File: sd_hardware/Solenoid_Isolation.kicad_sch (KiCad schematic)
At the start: 44 parts, among them Q1 RD3L08BGNTL, Q2 RD3L08BGNTL, Q3 RD3L08BGNTL, Q4 RD3L08BGNTL, Q5 RD3L08BGNTL, Q6 RD3L08BGNTL, Q7 RD3L08BGNTL, Q8 RD3L08BGNTL, U1 TLP291, U2 TLP291, U3 TLP291, U4 TLP291, U5 TLP291, U6 TLP291, U7 TLP291, U8 TLP291

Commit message: fix
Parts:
- D1: renamed from D3; footprint (none) -> LED_SMD:LED_0603_1608Metric_Pad1.05x0.95mm_HandSolder
- D10: renamed from D15; footprint (none) -> Diode_SMD:D_SOD-128
- D11: renamed from D8; footprint (none) -> Diode_SMD:D_SOD-128
- D12: renamed from D16; footprint (none) -> Diode_SMD:D_SOD-128
- D13: renamed from D9; footprint (none) -> Diode_SMD:D_SOD-128
- D14: renamed from D17; footprint (none) -> Diode_SMD:D_SOD-128
- D15: renamed from D10; footprint (none) -> Diode_SMD:D_SOD-128
- D16: renamed from D18; footprint (none) -> Diode_SMD:D_SOD-128
- D2: renamed from D11; footprint (none) -> LED_SMD:LED_0603_1608Metric_Pad1.05x0.95mm_HandSolder
- D3: renamed from D4; footprint (none) -> LED_SMD:LED_0603_1608Metric_Pad1.05x0.95mm_HandSolder
- D4: renamed from D12; footprint (none) -> LED_SMD:LED_0603_1608Metric_Pad1.05x0.95mm_HandSolder
- D5: footprint (none) -> LED_SMD:LED_0603_1608Metric_Pad1.05x0.95mm_HandSolder
- D6: renamed from D13; footprint (none) -> LED_SMD:LED_0603_1608Metric_Pad1.05x0.95mm_HandSolder
- D7: renamed from D6; footprint (none) -> LED_SMD:LED_0603_1608Metric_Pad1.05x0.95mm_HandSolder
- D8: renamed from D14; footprint (none) -> LED_SMD:LED_0603_1608Metric_Pad1.05x0.95mm_HandSolder
- D9: renamed from D7; footprint (none) -> Diode_SMD:D_SOD-128
- Q1, Q8: footprint (none) -> y-robo_footprint:TO252-3_ROM
- Q2: renamed from Q5; footprint (none) -> y-robo_footprint:TO252-3_ROM
- Q3: renamed from Q2; footprint (none) -> y-robo_footprint:TO252-3_ROM
- Q4: renamed from Q6; footprint (none) -> y-robo_footprint:TO252-3_ROM
- Q5: renamed from Q3; footprint (none) -> y-robo_footprint:TO252-3_ROM
- Q6: renamed from Q7; footprint (none) -> y-robo_footprint:TO252-3_ROM
- Q7: renamed from Q4; footprint (none) -> y-robo_footprint:TO252-3_ROM
- R1: renamed from R4; footprint (none) -> Resistor_SMD:R_0603_1608Metric_Pad0.98x0.95mm_HandSolder
- R2: renamed from R8; footprint (none) -> Resistor_SMD:R_0603_1608Metric_Pad0.98x0.95mm_HandSolder
- R3: renamed from R5; footprint (none) -> Resistor_SMD:R_0603_1608Metric_Pad0.98x0.95mm_HandSolder
- R4: renamed from R9; footprint (none) -> Resistor_SMD:R_0603_1608Metric_Pad0.98x0.95mm_HandSolder
- R5: renamed from R6; footprint (none) -> Resistor_SMD:R_0603_1608Metric_Pad0.98x0.95mm_HandSolder
- R6: renamed from R10; footprint (none) -> Resistor_SMD:R_0603_1608Metric_Pad0.98x0.95mm_HandSolder
- R7: footprint (none) -> Resistor_SMD:R_0603_1608Metric_Pad0.98x0.95mm_HandSolder
- R8: renamed from R11; footprint (none) -> Resistor_SMD:R_0603_1608Metric_Pad0.98x0.95mm_HandSolder
- RN1: renamed from RN2; footprint (none) -> Resistor_SMD:R_Array_Convex_8x0602
- RN2: renamed from RN1; footprint (none) -> Resistor_SMD:R_Array_Convex_8x0602
- RN3, RN4: footprint (none) -> Resistor_SMD:R_Array_Convex_8x0602
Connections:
- net FET1_Gate: now also RN3.9 (R8.2), RN4.1 (R1.1); no longer RN3.8 (R8.1), RN4.8 (R8.1)
- net FET2_Gate: now also Q2.1 (G), RN3.10 (R7.2), RN4.2 (R2.1); no longer Q3.1 (G), RN3.7 (R7.1), RN4.7 (R7.1)
- net FET3_Gate: now also Q3.1 (G), RN3.11 (R6.2), RN4.3 (R3.1); no longer Q5.1 (G), RN3.6 (R6.1), RN4.6 (R6.1)
- net FET4_Gate: now also Q4.1 (G), RN3.12 (R5.2), RN4.4 (R4.1); no longer Q7.1 (G), RN3.5 (R5.1), RN4.5 (R5.1)
- net FET5_Gate: now also Q5.1 (G), RN3.13 (R4.2), RN4.5 (R5.1); no longer Q2.1 (G), RN3.4 (R4.1), RN4.4 (R4.1)
- net FET6_Gate: now also Q6.1 (G), RN3.14 (R3.2), RN4.6 (R6.1); no longer Q4.1 (G), RN3.3 (R3.1), RN4.3 (R3.1)
- net FET7_Gate: now also Q7.1 (G), RN3.15 (R2.2), RN4.7 (R7.1); no longer Q6.1 (G), RN3.2 (R2.1), RN4.2 (R2.1)
- net FET8_Gate: now also RN3.16 (R1.2), RN4.8 (R8.1); no longer RN3.1 (R1.1), RN4.1 (R1.1)
- net GPIO1_IN: now also RN2.8 (R8.1); no longer RN2.9 (R8.2)
- net GPIO2_IN: now also RN2.7 (R7.1); no longer RN2.10 (R7.2)
- net GPIO3_IN: now also RN2.6 (R6.1); no longer RN2.11 (R6.2)
- net GPIO4_IN: now also RN2.5 (R5.1); no longer RN2.12 (R5.2)
- net GPIO5_IN: now also RN2.4 (R4.1); no longer RN2.13 (R4.2)
- net GPIO6_IN: now also RN2.3 (R3.1); no longer RN2.14 (R3.2)
- net GPIO7_IN: now also RN2.2 (R2.1); no longer RN2.15 (R2.2)
- net GPIO8_IN: now also RN2.1 (R1.1); no longer RN2.16 (R1.2)
- net Solenoid2_-: now also D10.2 (A), D2.1 (K), Q2.2 (D); no longer D11.2 (A), D3.1 (K), Q3.2 (D)
- net Solenoid3_-: now also D11.2 (A), D3.1 (K), Q3.2 (D); no longer D13.2 (A), D5.1 (K), Q5.2 (D)
- net Solenoid4_-: now also D12.2 (A), D4.1 (K), Q4.2 (D); no longer D15.2 (A), D7.1 (K), Q7.2 (D)
- net Solenoid5_-: now also D13.2 (A), D5.1 (K), Q5.2 (D); no longer D10.2 (A), D2.1 (K), Q2.2 (D)
- net Solenoid6_-: now also D14.2 (A), D6.1 (K), Q6.2 (D); no longer D12.2 (A), D4.1 (K), Q4.2 (D)
- net Solenoid7_-: now also D15.2 (A), D7.1 (K), Q7.2 (D); no longer D14.2 (A), D6.1 (K), Q6.2 (D)
- net at U2.1: now also RN2.10 (R7.2); no longer RN2.7 (R7.1)
- net at U2.3: now also RN3.7 (R7.1); no longer RN3.10 (R7.2)
- net at U8.1: now also RN2.16 (R1.2); no longer RN2.1 (R1.1)
- net at U7.1: now also RN2.15 (R2.2); no longer RN2.2 (R2.1)
- net at U6.1: now also RN2.14 (R3.2); no longer RN2.3 (R3.1)
- net at U5.1: now also RN2.13 (R4.2); no longer RN2.4 (R4.1)
- net at U4.1: now also RN2.12 (R5.2); no longer RN2.5 (R5.1)
- net at U3.1: now also RN2.11 (R6.2); no longer RN2.6 (R6.1)
- net at U1.1: now also RN2.9 (R8.2); no longer RN2.8 (R8.1)
- net at U3.3: now also RN3.6 (R6.1); no longer RN3.11 (R6.2)
- net at U4.3: now also RN3.5 (R5.1); no longer RN3.12 (R5.2)
- net at U5.3: now also RN3.4 (R4.1); no longer RN3.13 (R4.2)
- net at U6.3: now also RN3.3 (R3.1); no longer RN3.14 (R3.2)
- net at U7.3: now also RN3.2 (R2.1); no longer RN3.15 (R2.2)
- net at U8.3: now also RN3.1 (R1.1); no longer RN3.16 (R1.2)
- net at U1.3: now also RN3.8 (R8.1); no longer RN3.9 (R8.2)
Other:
- moved on the sheet: RN2, RN3, RN4

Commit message: fix var3.0 sd_hardware
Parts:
- removed RN3: 120_x8, Resistor_SMD:R_Array_Convex_8x0602, symbol Device:R_Pack08
- added R13, R14, R15, R16, R17, R18, R19, R20: 120, Resistor_SMD:R_0603_1608Metric_Pad0.98x0.95mm_HandSolder, symbol Device:R
- R1, R2, R3, R4, R5, R6, R7, R8: value 1k -> 1.5k
- renumbered RN4 to RN3
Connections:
- net FET1_Gate: now also R13.1
- net FET2_Gate: now also R14.1
- net FET3_Gate: now also R15.1
- net FET4_Gate: now also R16.1
- net FET5_Gate: now also R17.1
- net FET6_Gate: now also R18.1
- net FET7_Gate: now also R19.1
- net FET8_Gate: now also R20.1
- net at U2.3: now also R14.2
- net at U8.3: now also R20.2
- net at U7.3: now also R19.2
- net at U6.3: now also R18.2
- net at U5.3: now also R17.2
- net at U4.3: now also R16.2
- net at U3.3: now also R15.2
- net at U1.3: now also R13.2

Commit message: delete RN
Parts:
- removed RN1: 1k_x8, Resistor_SMD:R_Array_Convex_8x0602, symbol Device:R_Pack08
- removed RN2: 330_x8, Resistor_SMD:R_Array_Convex_8x0602, symbol Device:R_Pack08
- removed RN3: 10k_x08, Resistor_SMD:R_Array_Convex_8x0602, symbol Device:R_Pack08
- added R22, R23, R24, R25, R26, R27, R28, R29: 330, Resistor_SMD:R_0603_1608Metric_Pad0.98x0.95mm_HandSolder, symbol Device:R
- added R30, R31, R32, R33, R34, R35, R36, R37: 1k, Resistor_SMD:R_0603_1608Metric_Pad0.98x0.95mm_HandSolder, symbol Device:R
- added R38, R39, R40, R41, R42, R43, R44, R45: 10k, Resistor_SMD:R_0603_1608Metric_Pad0.98x0.95mm_HandSolder, symbol Device:R
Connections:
- net +12V: now also R30.1, R31.1, R32.1, R33.1, R34.1, R35.1, R36.1, R37.1
- net FET1_Gate: now also R38.2
- net FET2_Gate: now also R39.2
- net FET3_Gate: now also R40.2
- net FET4_Gate: now also R41.2
- net FET5_Gate: now also R45.2
- net FET6_Gate: now also R44.2
- net FET7_Gate: now also R43.2
- net FET8_Gate: now also R42.2
- net GNDPWR: now also R38.1, R39.1, R40.1, R41.1, R42.1, R43.1, R44.1, R45.1
- net GPIO1_IN: now also R22.2
- net GPIO2_IN: now also R23.2
- net GPIO3_IN: now also R24.2
- net GPIO4_IN: now also R25.2
- net GPIO5_IN: now also R26.2
- net GPIO6_IN: now also R27.2
- net GPIO7_IN: now also R28.2
- net GPIO8_IN: now also R29.2
- net at U2.1: now also R23.1
- net at U2.4: now also R37.2
- net at U3.1: now also R24.1
- net at U4.1: now also R25.1
- net at U5.1: now also R26.1
- net at U6.1: now also R27.1
- net at U7.1: now also R28.1
- net at U8.1: now also R29.1
- net at U1.1: now also R22.1
- net at U3.4: now also R34.2
- net at U4.4: now also R35.2
- net at U8.4: now also R30.2
- net at U5.4: now also R32.2
- net at U6.4: now also R33.2
- net at U7.4: now also R31.2
- net at U1.4: now also R36.2

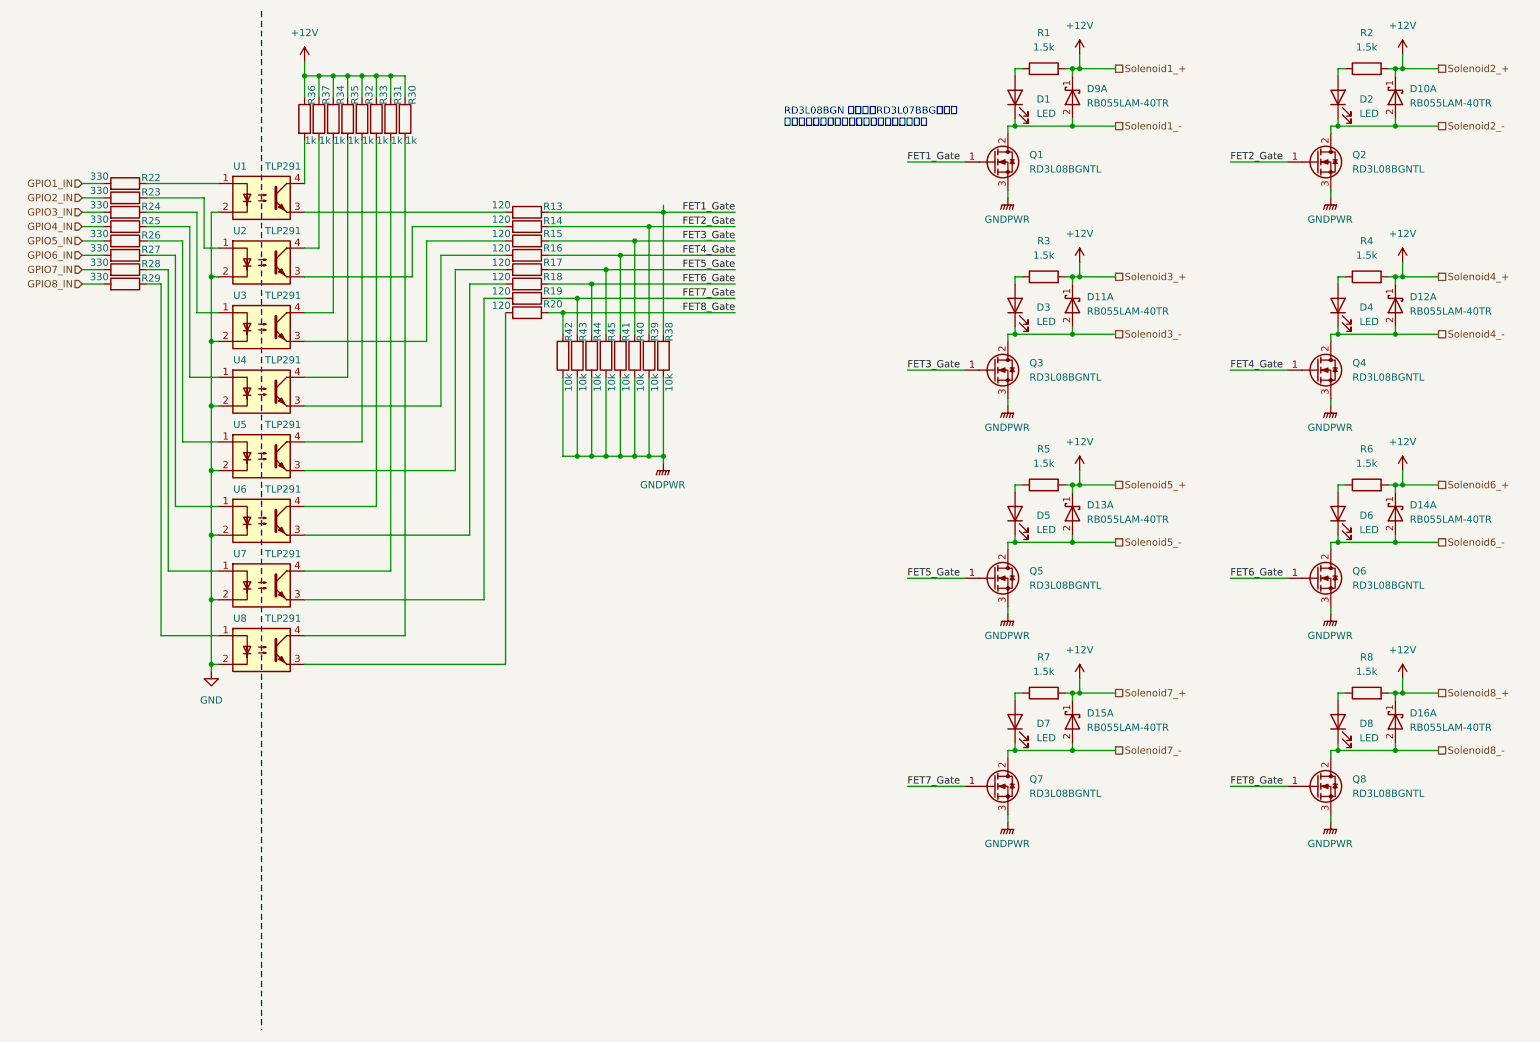
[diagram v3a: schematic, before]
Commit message: Change to Photo Relay
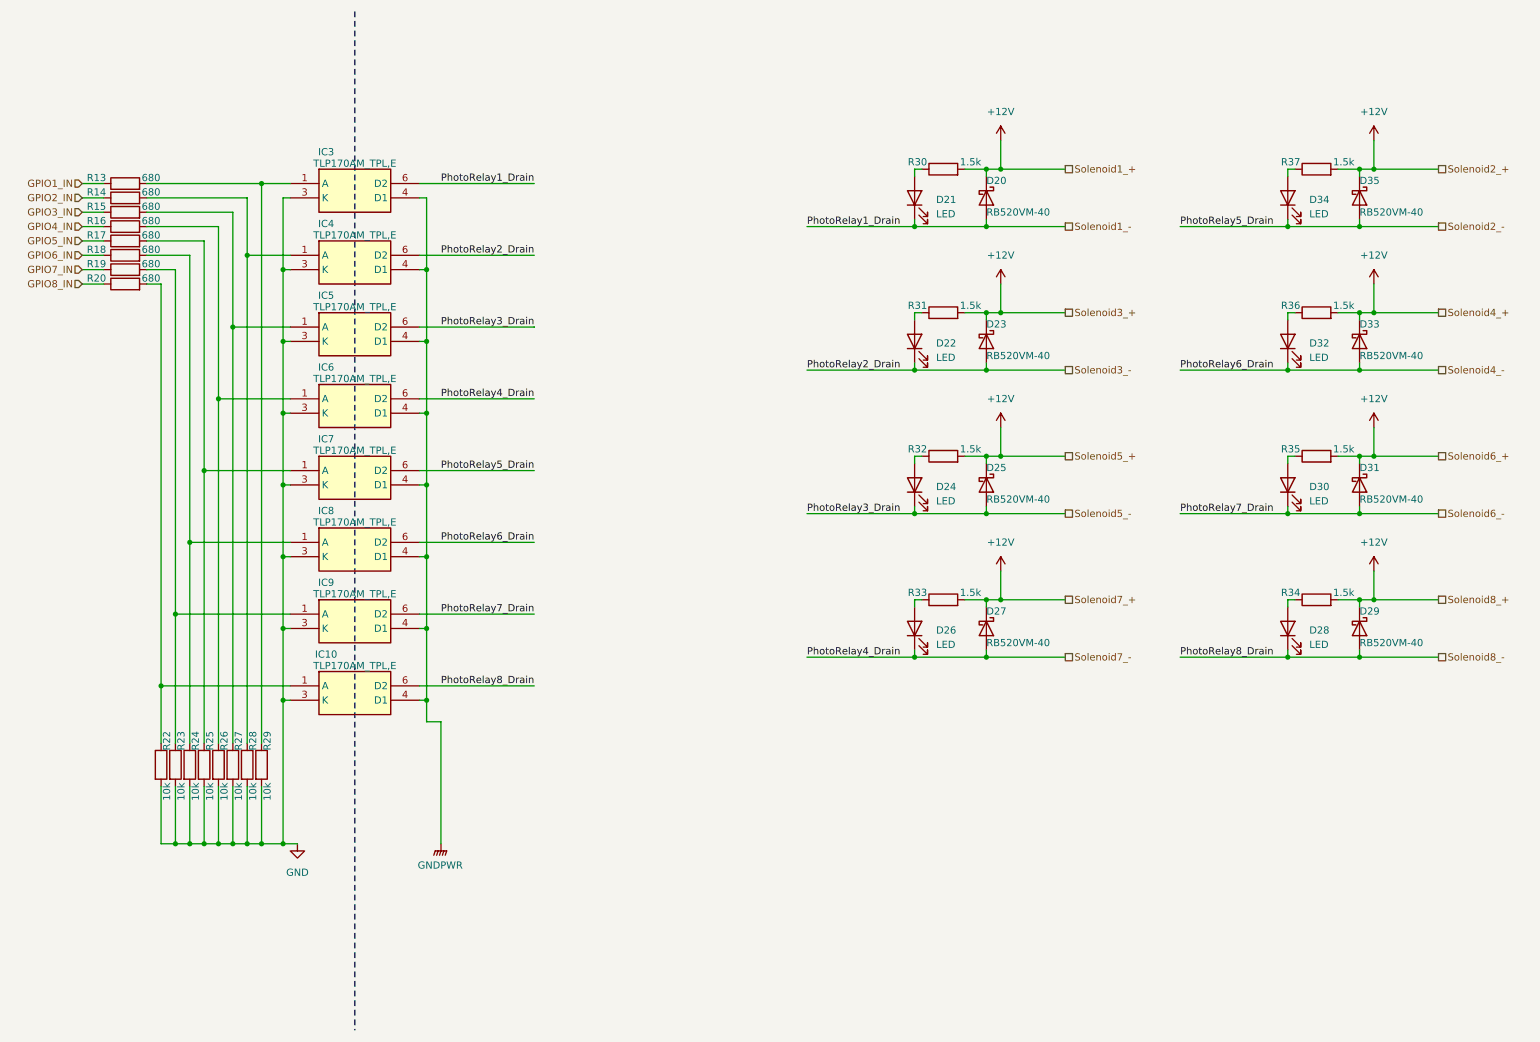
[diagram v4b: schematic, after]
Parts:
- removed D1, D2, D3, D4, D5, D6, D7, D8: LED, LED_SMD:LED_0603_1608Metric_Pad1.05x0.95mm_HandSolder, symbol Device:LED
- removed D10, D11, D12, D13, D14, D15, D16, D9: RB055LAM-40TR, Diode_SMD:D_SOD-128, symbol Device:D_Schottky_Dual_CommonAnode_KAK_Split
- removed Q1, Q2, Q3, Q4, Q5, Q6, Q7, Q8: RD3L08BGNTL, y-robo_footprint:TO252-3_ROM, symbol Transistor_FET:Q_NMOS_GDS
- removed R1, R2, R3, R4, R5, R6, R7, R8: 1.5k, Resistor_SMD:R_0603_1608Metric_Pad0.98x0.95mm_HandSolder, symbol Device:R
- removed R38, R39, R40, R41, R42, R43, R44, R45: 10k, Resistor_SMD:R_0603_1608Metric_Pad0.98x0.95mm_HandSolder, symbol Device:R
- removed U1, U2, U3, U4, U5, U6, U7, U8: TLP291, Package_SO:SOIC-4_4.55x2.6mm_P1.27mm, symbol Isolator:TLP291
- added D20, D23, D25, D27, D29, D31, D33, D35: RB520VM-40, Diode_THT:Diode_Bridge_Round_D9.0mm, symbol Device:D_Schottky
- added D21, D22, D24, D26, D28, D30, D32, D34: LED, LED_SMD:LED_0603_1608Metric_Pad1.05x0.95mm_HandSolder, symbol Device:LED
- added IC10, IC3, IC4, IC5, IC6, IC7, IC8, IC9: TLP170AM_TPL,E, TLP170AMTPLE, symbol TLP170AM_TPL_E:TLP170AM_TPL,E
- R13, R14, R15, R16, R17, R18, R19, R20: value 120 -> 680; footprint Resistor_SMD:R_0603_1608Metric_Pad0.98x0.95mm_HandSolder -> TLP170AMTPLE
- R22, R23, R24, R25, R26, R27, R28, R29: value 330 -> 10k; footprint Resistor_SMD:R_0603_1608Metric_Pad0.98x0.95mm_HandSolder -> TLP170AMTPLE
- R30, R31, R32, R33, R34, R35, R36, R37: value 1k -> 1.5k
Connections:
- net FET1_Gate is gone; now on net GPIO1_IN: R13.1
- net FET2_Gate is gone; now on net GPIO2_IN: R14.1
- net FET3_Gate is gone; now on net GPIO3_IN: R15.1
- net FET4_Gate is gone; now on net GPIO4_IN: R16.1
- net FET5_Gate is gone; now on net GPIO5_IN: R17.1
- net FET6_Gate is gone; now on net GPIO6_IN: R18.1
- net FET7_Gate is gone; now on net GPIO7_IN: R19.1
- net FET8_Gate is gone; now on net GPIO8_IN: R20.1
- net +12V: now also R30.2, R31.2, R32.2, R33.2, R34.2, R35.2, R36.2, R37.2, D20.1 (K), D23.1 (K), D25.1 (K), D27.1 (K), D29.1 (K), D31.1 (K), D33.1 (K), D35.1 (K); no longer R30.1, R31.1, R32.1, R33.1, R34.1, R35.1, R36.1, R37.1
- net GND: now also R22.2, R23.2, R24.2, R25.2, R26.2, R27.2, R28.2, R29.2, IC10.3 (K), IC3.3 (K), IC4.3 (K), IC5.3 (K), IC6.3 (K), IC7.3 (K), IC8.3 (K), IC9.3 (K)
- net GNDPWR: now also IC10.4 (D1), IC3.4 (D1), IC4.4 (D1), IC5.4 (D1), IC6.4 (D1), IC7.4 (D1), IC8.4 (D1), IC9.4 (D1)
- net GPIO1_IN: no longer R22.2
- net GPIO2_IN: no longer R23.2
- net GPIO3_IN: no longer R24.2
- net GPIO4_IN: no longer R25.2
- net GPIO5_IN: no longer R26.2
- net GPIO6_IN: no longer R27.2
- net GPIO7_IN: no longer R28.2
- net GPIO8_IN: no longer R29.2
- net Solenoid1_-: now also D20.2 (A), D21.1 (K), IC3.6 (D2)
- net Solenoid2_-: now also D34.1 (K), D35.2 (A), IC7.6 (D2)
- net Solenoid3_-: now also D22.1 (K), D23.2 (A), IC4.6 (D2)
- net Solenoid4_-: now also D32.1 (K), D33.2 (A), IC8.6 (D2)
- net Solenoid5_-: now also D24.1 (K), D25.2 (A), IC5.6 (D2)
- net Solenoid6_-: now also D30.1 (K), D31.2 (A), IC9.6 (D2)
- net Solenoid7_-: now also D26.1 (K), D27.2 (A), IC6.6 (D2)
- net Solenoid8_-: now also D28.1 (K), D29.2 (A), IC10.6 (D2)
- net at R15.2: now also R27.1, IC5.1 (A)
- net at R17.2: now also R25.1, IC7.1 (A)
- net at R13.2: now also R29.1, IC3.1 (A)
- net at R23.1: now also R19.2, IC9.1 (A)
- net at R14.2: now also R28.1, IC4.1 (A)
- net at R18.2: now also R24.1, IC8.1 (A)
- net at R16.2: now also R26.1, IC6.1 (A)
- net at R22.1: now also R20.2, IC10.1 (A)
- new net: D34.2 (A), R37.1
- new net: D21.2 (A), R30.1
- new net: D28.2 (A), R34.1
- new net: D24.2 (A), R32.1
- new net: D32.2 (A), R36.1
- new net: D26.2 (A), R33.1
- new net: D30.2 (A), R35.1
- new net: D22.2 (A), R31.1
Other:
- note removed: "RD3L08BGN は終売，RD3L07BBGが推奨 パッケージ同等なためおそらく問題ないはず"
